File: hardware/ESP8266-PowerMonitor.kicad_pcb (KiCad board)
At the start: 2 copper layers, 69.5 x 27.2 mm, 20 parts, among them J1 CONN_PULSE, J2 CONN_PROG, J3 CONN_AC, J4 CONN_TEMP, J5 CONN_I2C, SW1 SW_RESET, U1 AMS1117-3.3, U2 ESP-12F

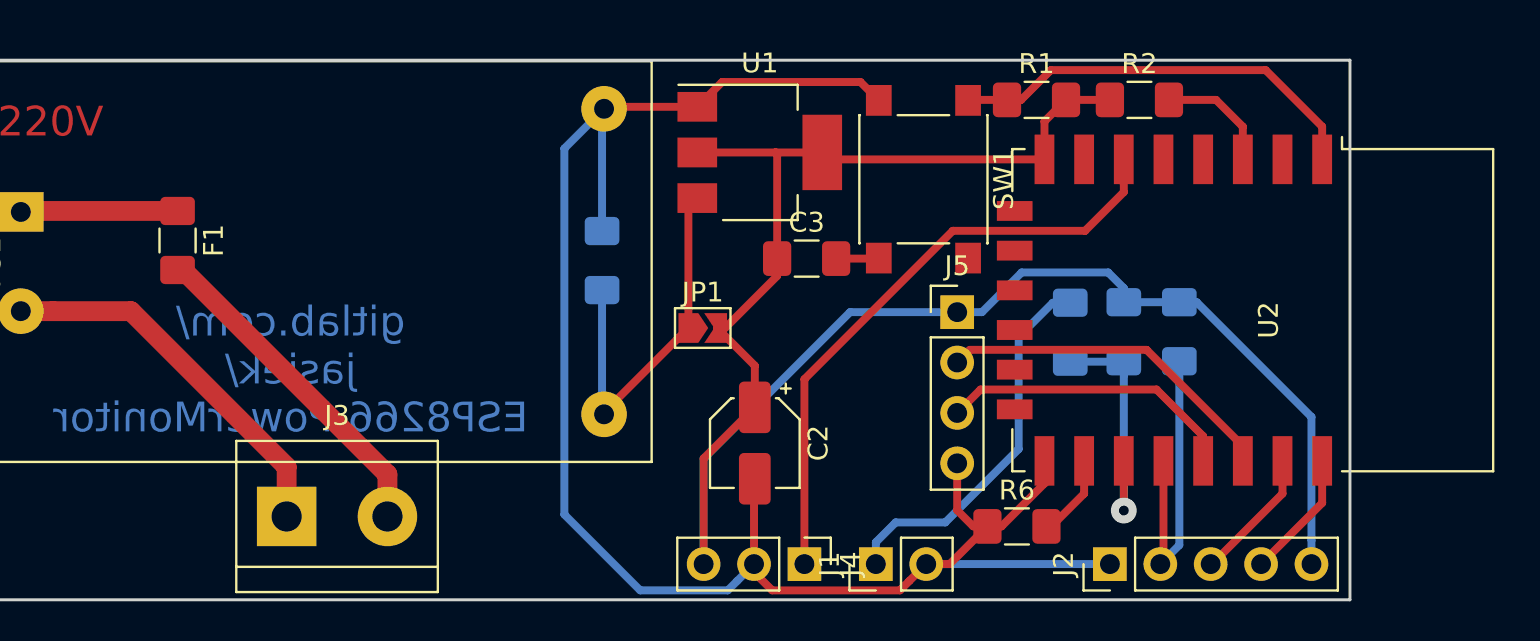
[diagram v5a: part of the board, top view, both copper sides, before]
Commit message: Updated PCB, uses GPIO13 instead of GPIO2, which didn't work.
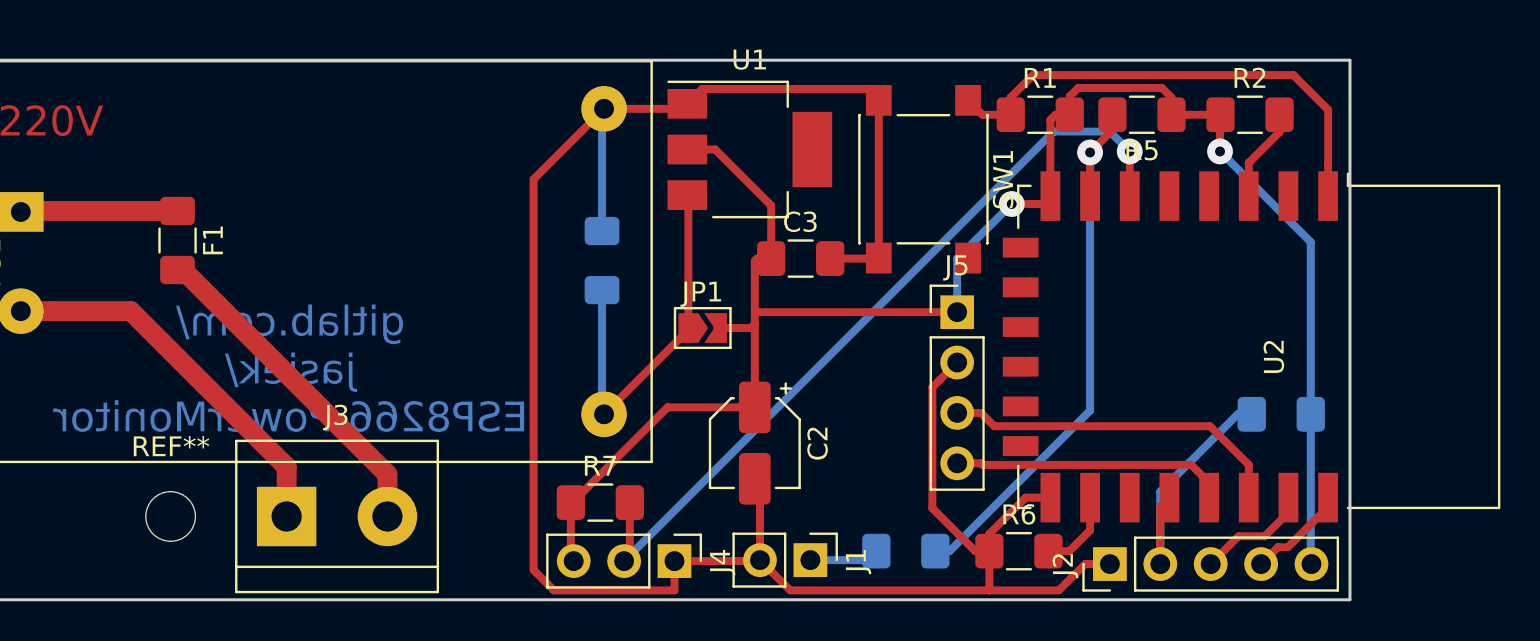
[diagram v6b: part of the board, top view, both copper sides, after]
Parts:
- added R7: 4.7k, Resistor_SMD:R_1206_3216Metric_Pad1.42x1.75mm_HandSolder, F.Cu at (139.3, 113.1)
- added REF**: MountingHole_2.5mm, MountingHole:MountingHole_2.5mm, F.Cu at (117.7, 113.8)
- R5: moved to F.Cu
- moved R3 13.8 mm to (154.7, 115.5), turned to 180 degrees
- moved R5 11.0 mm to (166.6, 93.5), turned to 180 degrees
- moved R4 6.61 mm to (173.6, 108.7), turned to 180 degrees
- moved J4 6.55 mm to (143.1, 116.0)
- moved R2 5.63 mm to (172.1, 93.5)
- moved J1 3.31 mm to (149.9, 116.0), turned to 270 degrees
- moved U2 1.87 mm to (172.5, 105.2)
- moved R6 1.25 mm to (160.4, 115.5)
- moved R1 0.77 mm to (161.5, 93.5)
- moved U1 0.52 mm to (146.8, 95.3)
- moved C3 0.30 mm to (149.4, 100.8)
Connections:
- J4 pad 1: DS18B20_DQ -> GND
- J4 pad 2: GND -> DS18B20_DQ
- J5 pad 2: SCL -> GND
- J5 pad 3: SDA -> SCL
- J5 pad 4: GND -> SDA
- U2 pad 17: Net-(R3-Pad1) -> (no net)
- U2 pad 7: (no net) -> Net-(R3-Pad1)
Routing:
- net GND: track 92.7 -> 110.6 mm
- net PULSE: track 19.2 -> 3.51 mm
- net Net-(R3-Pad1): track 12.7 -> 28.3 mm
- net DS18B20_DQ: track 31.0 -> 40.2 mm, vias 0 -> 1
- net +3.3V: track 98.1 -> 90.8 mm, vias 0 -> 2
- net Net-(R1-Pad1): track 21.3 -> 24.9 mm
- net _PROG: track 16.2 -> 13.4 mm
- net SDA: track 15.9 -> 13.9 mm
- net TXD: track 6.48 -> 5.04 mm
- net Net-(R2-Pad2): track 5.93 -> 4.74 mm
- net RXD: track 6.74 -> 5.75 mm

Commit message: Revision 2 PCB done.
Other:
- board text added: "gitlab.com/ jasiek/ ESP8266-PowerMonitor rev 2"
- board text removed: "gitlab.com/ jasiek/ ESP8266-PowerMonitor"
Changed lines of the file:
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@@
     (add_net "Net-(R3-Pad1)")
     (add_net "Net-(R6-Pad2)")
-    (add_net "Net-(U2-Pad10)")
-    (add_net "Net-(U2-Pad11)")
-    (add_net "Net-(U2-Pad12)")
-    (add_net "Net-(U2-Pad13)")
-    (add_net "Net-(U2-Pad14)")
-    (add_net "Net-(U2-Pad17)")
-    (add_net "Net-(U2-Pad2)")
-    (add_net "Net-(U2-Pad4)")
-    (add_net "Net-(U2-Pad5)")
-    (add_net "Net-(U2-Pad9)")
     (add_net PULSE)
     (add_net RXD)
@@
     (effects (font (size 1.5 1.5) (thickness 0.3)))
   )
-  (gr_text "gitlab.com/\njasiek/\nESP8266-PowerMonitor" (at 123.7 106.4) (layer B.Cu)
+  (gr_text "gitlab.com/\njasiek/\nESP8266-PowerMonitor\n\nrev 2" (at 125.4 105.05) (layer B.Cu)
     (effects (font (size 1.5 1.5) (thickness 0.3)) (justify mirror))
   )
